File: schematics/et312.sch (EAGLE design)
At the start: 0 parts

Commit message: PCB WIP
Layed down uC and some other componants
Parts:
- added 10WAY_RIBBON: M10SILK_FEMALE_PTH, SparkFun-Connectors:M10SILK_FEMALE_PTH
- added IC1: MEGA8-P, atmel:MEGA8-P
- added S2, S4: SPST, adafruit:SPST
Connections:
- new net GND: IC1.GND, IC1.GND@1
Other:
- note added: "Menu"
- note added: "Small PCB"
- note added: "Up"
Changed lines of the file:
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@@
 <layer number="54" name="bGND_GNDA" color="1" fill="9" visible="no" active="no"/>
 <layer number="56" name="wert" color="7" fill="1" visible="no" active="no"/>
+<layer number="57" name="tCAD" color="7" fill="1" visible="no" active="no"/>
+<layer number="90" name="Modules" color="5" fill="1" visible="yes" active="yes"/>
 <layer number="91" name="Nets" color="2" fill="1" visible="yes" active="yes"/>
 <layer number="92" name="Busses" color="1" fill="1" visible="yes" active="yes"/>
@@
 <layer number="97" name="Info" color="7" fill="1" visible="yes" active="yes"/>
 <layer number="98" name="Guide" color="6" fill="1" visible="yes" active="yes"/>
+<layer number="99" name="SpiceOrder" color="7" fill="1" visible="no" active="no"/>
 <layer number="100" name="Muster" color="7" fill="1" visible="no" active="no"/>
 <layer number="101" name="Patch_Top" color="12" fill="4" visible="yes" active="yes"/>
@@
 <layer number="111" name="LPC17xx" color="7" fill="1" visible="yes" active="yes"/>
 <layer number="112" name="tSilk" color="7" fill="1" visible="yes" active="yes"/>
+<layer number="113" name="IDFDebug" color="4" fill="1" visible="yes" active="yes"/>
 <layer number="116" name="Patch_BOT" color="9" fill="4" visible="yes" active="yes"/>
 <layer number="121" name="_tsilk" color="7" fill="1" visible="yes" active="yes"/>
@@
 <layer number="132" name="bAdjust" color="7" fill="1" visible="no" active="yes"/>
 <layer number="144" name="Drill_legend" color="7" fill="1" visible="yes" active="yes"/>
+<layer number="150" name="Notes" color="7" fill="1" visible="yes" active="yes"/>
 <layer number="151" name="HeatSink" color="7" fill="1" visible="yes" active="yes"/>
 <layer number="152" name="_bDocu" color="7" fill="1" visible="yes" active="yes"/>
+<layer number="153" name="FabDoc1" color="7" fill="1" visible="yes" active="yes"/>
+<layer number="154" name="FabDoc2" color="7" fill="1" visible="yes" active="yes"/>
+<layer number="155" name="FabDoc3" color="7" fill="1" visible="yes" active="yes"/>
 <layer number="199" name="Contour" color="7" fill="1" visible="yes" active="yes"/>
 <layer number="200" name="200bmp" color="1" fill="10" visible="yes" active="yes"/>
@@
 <part name="FRAME2" library="frames" deviceset="A4L-LOC" device=""/>
 <part name="FRAME1" library="frames" deviceset="A4L-LOC" device=""/>
+<part name="IC1" library="atmel" deviceset="MEGA8-P" device=""/>
+<part name="GND1" library="SparkFun-Aesthetics" deviceset="GND" device=""/>
+<part name="FRAME3" library="frames" deviceset="A4L-LOC" device=""/>
+<part name="S2" library="adafruit" deviceset="SPST" device=""/>
+<part name="S4" library="adafruit" deviceset="SPST" device=""/>
+<part name="10WAY_RIBBON" library="SparkFun-Connectors" deviceset="M10" device="SILK_FEMALE_PTH"/>
 </parts>
 <sheets>
@@
 <instances>
 <instance part="FRAME1" gate="G$1" x="0" y="0"/>
+<instance part="IC1" gate="G$1" x="127" y="93.98"/>
+<instance part="GND1" gate="1" x="88.9" y="30.48"/>
 </instances>
 <busses>
+</busses>
+<nets>
+<net name="GND" class="0">
+<segment>
+<pinref part="GND1" gate="1" pin="GND"/>
+<wire x1="88.9" y1="33.02" x2="88.9" y2="91.44" width="0.1524" layer="91"/>
+<pinref part="IC1" gate="G$1" pin="GND@1"/>
+<wire x1="88.9" y1="91.44" x2="104.14" y2="91.44" width="0.1524" layer="91"/>
+<pinref part="IC1" gate="G$1" pin="GND"/>
+<wire x1="104.14" y1="116.84" x2="88.9" y2="116.84" width="0.1524" layer="91"/>
+<wire x1="88.9" y1="116.84" x2="88.9" y2="91.44" width="0.1524" layer="91"/>
+<junction x="88.9" y="91.44"/>
+</segment>
+</net>
+</nets>
+</sheet>
+<sheet>
+<plain>
+<text x="162.56" y="20.32" size="1.778" layer="91">Small PCB</text>
+<text x="86.36" y="134.62" size="1.778" layer="91">Menu</text>
+<text x="86.36" y="104.14" size="1.778" layer="91">Up</text>
+</plain>
+<instances>
+<instance part="FRAME3" gate="G$1" x="0" y="0"/>
+<instance part="S2" gate="G$1" x="86.36" y="142.24" rot="R270"/>
+<instance part="S4" gate="G$1" x="86.36" y="111.76" rot="R270"/>
+<instance part="10WAY_RIBBON" gate="G$1" x="12.7" y="157.48"/>
+</instances>
+<busses>

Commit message: Added small board
Added 2 buttons, and two pots to the small board, found the CD4066 in dip, and added to new sheet.
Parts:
- added 10WAY_RIBBON1: M10SILK_FEMALE_PTH, SparkFun-Connectors:M10SILK_FEMALE_PTH
- added IC2: 4066N, 40xx:4066N
- added RV1, RV2: (no value), SparkFun-Electromechanical:POT
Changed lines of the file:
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@@
 <part name="S4" library="adafruit" deviceset="SPST" device=""/>
 <part name="10WAY_RIBBON" library="SparkFun-Connectors" deviceset="M10" device="SILK_FEMALE_PTH"/>
+<part name="FRAME4" library="frames" deviceset="A4L-LOC" device=""/>
+<part name="IC2" library="40xx" deviceset="4066" device="N"/>
+<part name="10WAY_RIBBON1" library="SparkFun-Connectors" deviceset="M10" device="SILK_FEMALE_PTH"/>
+<part name="RV1" library="SparkFun-Electromechanical" deviceset="POT" device=""/>
+<part name="RV2" library="SparkFun-Electromechanical" deviceset="POT" device=""/>
 </parts>
 <sheets>
@@
 <instance part="S4" gate="G$1" x="86.36" y="111.76" rot="R270"/>
 <instance part="10WAY_RIBBON" gate="G$1" x="12.7" y="157.48"/>
+<instance part="RV1" gate="G$1" x="83.82" y="63.5"/>
+<instance part="RV2" gate="G$1" x="83.82" y="33.02"/>
 </instances>
 <busses>
+</busses>
+<nets>
+</nets>
+</sheet>
+<sheet>
+<plain>
+</plain>
+<instances>
+<instance part="FRAME4" gate="G$1" x="0" y="0"/>
+<instance part="IC2" gate="A" x="83.82" y="139.7"/>
+<instance part="IC2" gate="B" x="157.48" y="139.7"/>
+<instance part="IC2" gate="C" x="83.82" y="96.52"/>
+<instance part="IC2" gate="D" x="157.48" y="96.52"/>
+<instance part="10WAY_RIBBON1" gate="G$1" x="10.922" y="159.004"/>
+</instances>
+<busses>

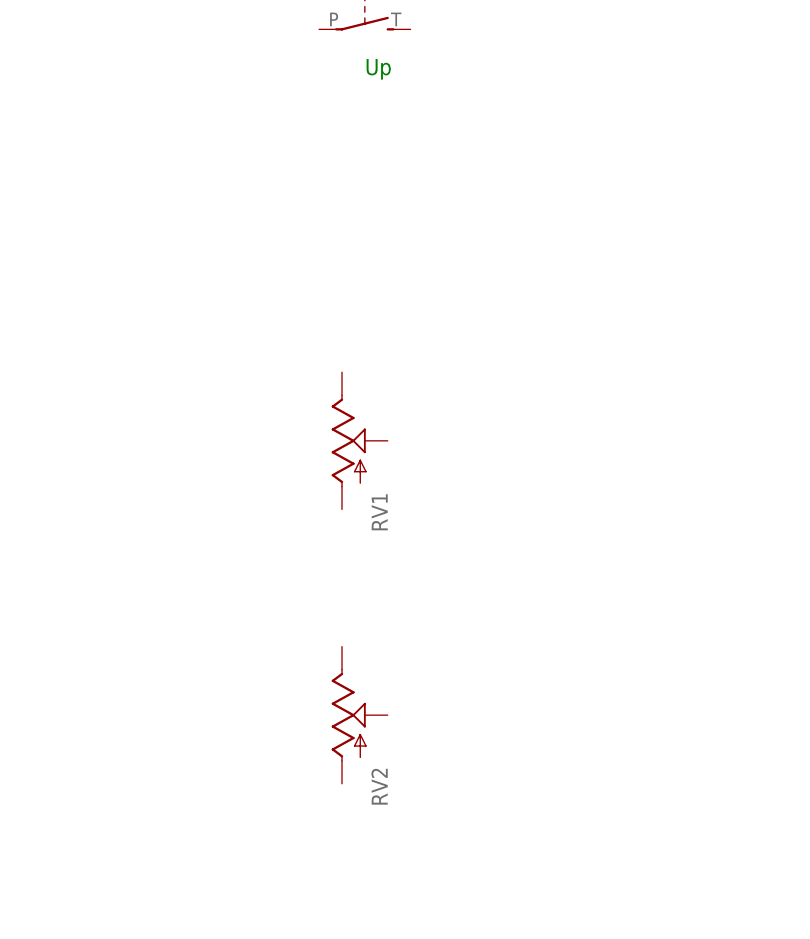
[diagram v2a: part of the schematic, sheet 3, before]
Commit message: CDB4066 added
Control pins are listed as connected to pin 22 on uC, 22 is listed as a ground… can some one please check!
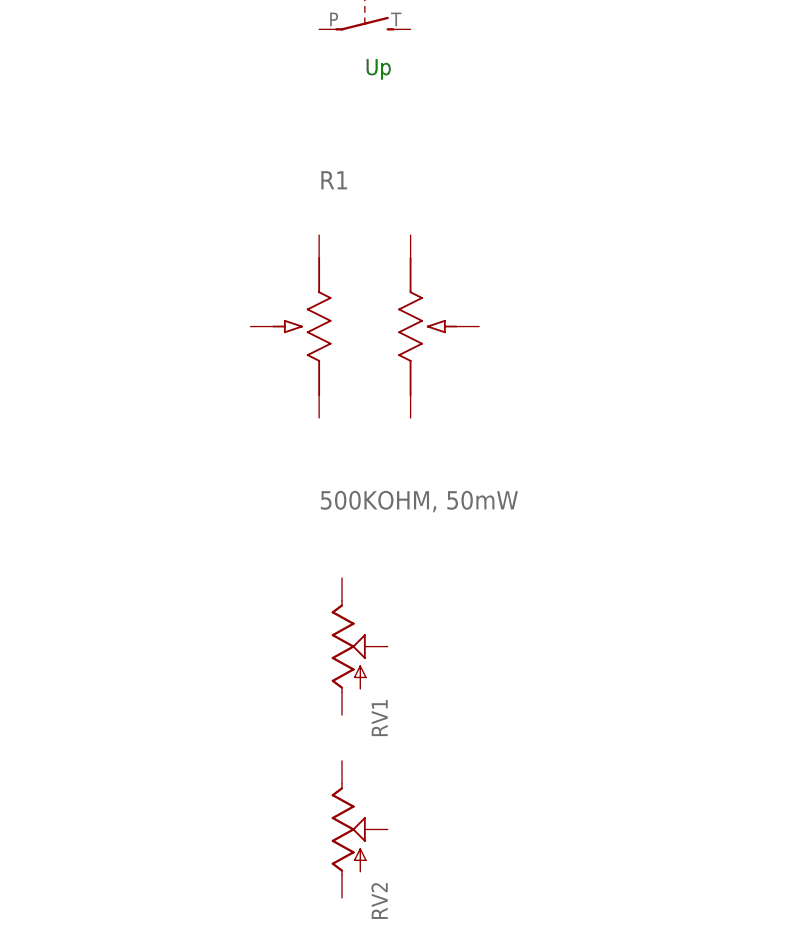
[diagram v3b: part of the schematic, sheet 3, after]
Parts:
- added R1: 500KOHM, 50mW, Panasonic-Trimmer_Potentiometers:EVJC20F02A14-JC2
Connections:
- net GND: now also IC2A.C, IC2B.C, IC2C.C, IC2D.C
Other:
- moved on the sheet: RV1, RV2
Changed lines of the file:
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@@
 <part name="RV1" library="SparkFun-Electromechanical" deviceset="POT" device=""/>
 <part name="RV2" library="SparkFun-Electromechanical" deviceset="POT" device=""/>
+<part name="R1" library="Panasonic-Trimmer_Potentiometers" deviceset="EVJ" device="-JC2" technology="C20F02A14" value="500KOHM, 50mW"/>
+<part name="GND2" library="SparkFun-Aesthetics" deviceset="GND" device=""/>
+<part name="GND3" library="SparkFun-Aesthetics" deviceset="GND" device=""/>
+<part name="GND4" library="SparkFun-Aesthetics" deviceset="GND" device=""/>
+<part name="GND5" library="SparkFun-Aesthetics" deviceset="GND" device=""/>
 </parts>
 <sheets>
@@
 <instance part="S4" gate="G$1" x="86.36" y="111.76" rot="R270"/>
 <instance part="10WAY_RIBBON" gate="G$1" x="12.7" y="157.48"/>
-<instance part="RV1" gate="G$1" x="83.82" y="63.5"/>
-<instance part="RV2" gate="G$1" x="83.82" y="33.02"/>
+<instance part="RV1" gate="G$1" x="83.82" y="40.64"/>
+<instance part="RV2" gate="G$1" x="83.82" y="20.32"/>
+<instance part="R1" gate="A" x="86.36" y="76.2"/>
 </instances>
 <busses>
@@
 <instance part="IC2" gate="D" x="157.48" y="96.52"/>
 <instance part="10WAY_RIBBON1" gate="G$1" x="10.922" y="159.004"/>
+<instance part="GND2" gate="1" x="68.58" y="86.36"/>
+<instance part="GND3" gate="1" x="68.58" y="129.54"/>
+<instance part="GND4" gate="1" x="142.24" y="129.54"/>
+<instance part="GND5" gate="1" x="142.24" y="86.36"/>
 </instances>
 <busses>
 </busses>
 <nets>
+<net name="GND" class="0">
+<segment>
+<pinref part="GND2" gate="1" pin="GND"/>
+<pinref part="IC2" gate="C" pin="C"/>
+<wire x1="68.58" y1="88.9" x2="68.58" y2="93.98" width="0.1524" layer="91"/>
+<wire x1="68.58" y1="93.98" x2="71.12" y2="93.98" width="0.1524" layer="91"/>
+</segment>
+<segment>
+<pinref part="IC2" gate="A" pin="C"/>
+<wire x1="71.12" y1="137.16" x2="68.58" y2="137.16" width="0.1524" layer="91"/>
+<pinref part="GND3" gate="1" pin="GND"/>
+<wire x1="68.58" y1="137.16" x2="68.58" y2="132.08" width="0.1524" layer="91"/>
+</segment>
+<segment>
+<pinref part="GND4" gate="1" pin="GND"/>
+<wire x1="142.24" y1="132.08" x2="142.24" y2="137.16" width="0.1524" layer="91"/>
+<pinref part="IC2" gate="B" pin="C"/>
+<wire x1="142.24" y1="137.16" x2="144.78" y2="137.16" width="0.1524" layer="91"/>
+</segment>
+<segment>
+<pinref part="IC2" gate="D" pin="C"/>
+<wire x1="144.78" y1="93.98" x2="142.24" y2="93.98" width="0.1524" layer="91"/>
+<pinref part="GND5" gate="1" pin="GND"/>
+<wire x1="142.24" y1="93.98" x2="142.24" y2="88.9" width="0.1524" layer="91"/>
+</segment>
+</net>
 </nets>
 </sheet>

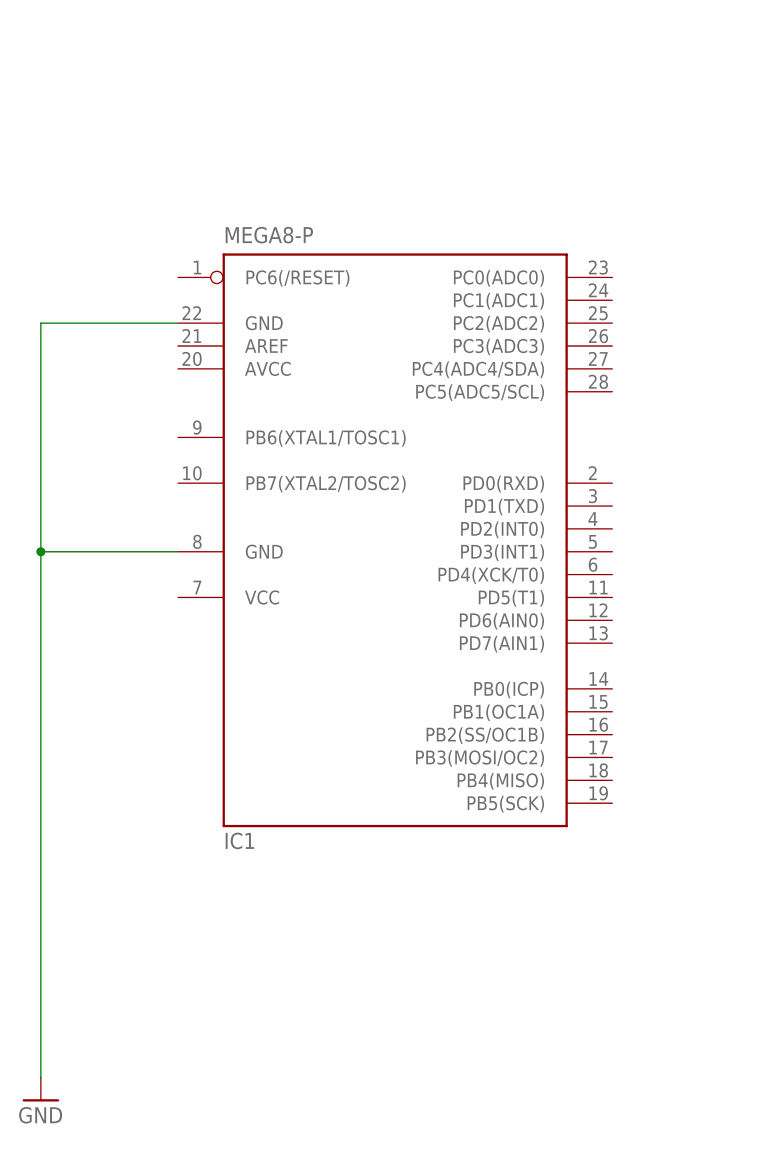
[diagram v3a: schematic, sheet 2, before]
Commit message: fixed uC
picked up a atmega16 rather than atmega8
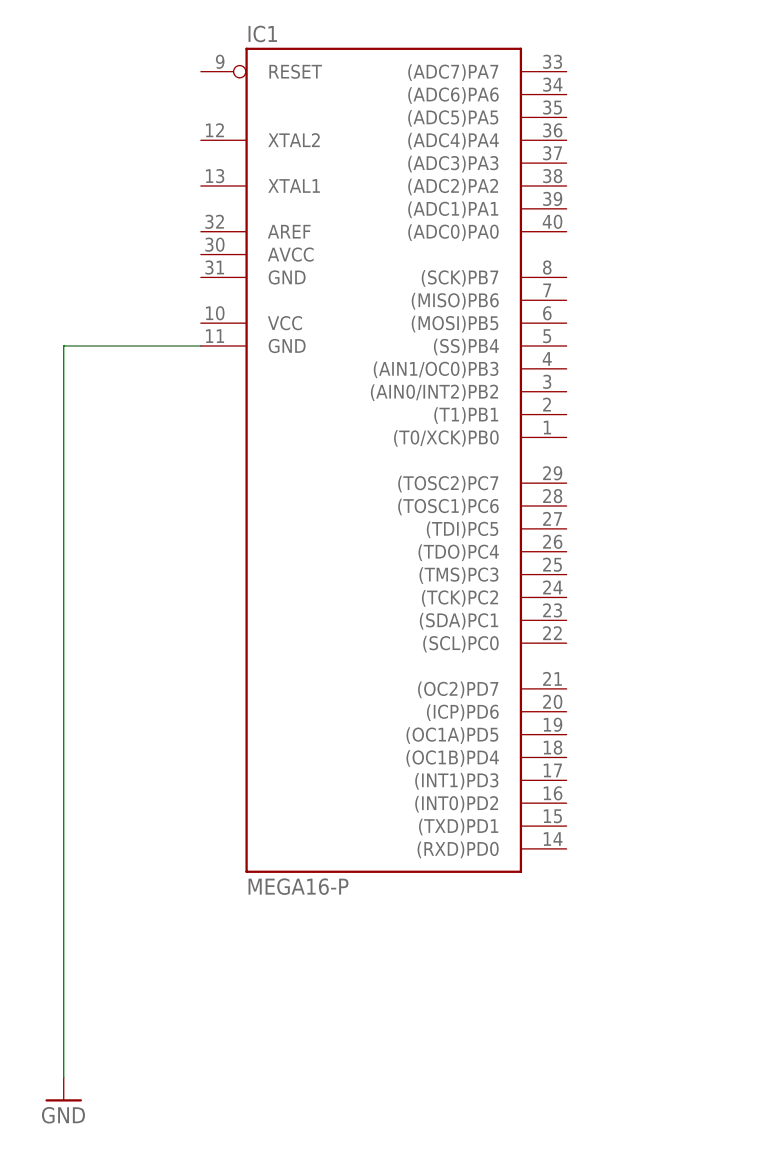
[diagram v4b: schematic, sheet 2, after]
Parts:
- IC1: value MEGA8-P -> MEGA16-P; device atmel:MEGA8-P -> atmel:MEGA16-P
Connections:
- net GND: no longer IC1.GND@1
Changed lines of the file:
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@@
 <part name="FRAME2" library="frames" deviceset="A4L-LOC" device=""/>
 <part name="FRAME1" library="frames" deviceset="A4L-LOC" device=""/>
-<part name="IC1" library="atmel" deviceset="MEGA8-P" device=""/>
 <part name="GND1" library="SparkFun-Aesthetics" deviceset="GND" device=""/>
 <part name="FRAME3" library="frames" deviceset="A4L-LOC" device=""/>
@@
 <part name="GND4" library="SparkFun-Aesthetics" deviceset="GND" device=""/>
 <part name="GND5" library="SparkFun-Aesthetics" deviceset="GND" device=""/>
+<part name="IC1" library="atmel" deviceset="MEGA16-P" device=""/>
 </parts>
 <sheets>
@@
 <instances>
 <instance part="FRAME1" gate="G$1" x="0" y="0"/>
-<instance part="IC1" gate="G$1" x="127" y="93.98"/>
-<instance part="GND1" gate="1" x="88.9" y="30.48"/>
+<instance part="GND1" gate="1" x="91.44" y="30.48"/>
+<instance part="IC1" gate="G$1" x="127" y="104.14"/>
 </instances>
 <busses>
@@
 <net name="GND" class="0">
 <segment>
+<pinref part="IC1" gate="G$1" pin="GND"/>
+<wire x1="106.68" y1="114.3" x2="91.44" y2="114.3" width="0.1524" layer="91"/>
+<wire x1="91.44" y1="114.3" x2="91.44" y2="33.02" width="0.1524" layer="91"/>
 <pinref part="GND1" gate="1" pin="GND"/>
-<wire x1="88.9" y1="33.02" x2="88.9" y2="91.44" width="0.1524" layer="91"/>
-<pinref part="IC1" gate="G$1" pin="GND@1"/>
-<wire x1="88.9" y1="91.44" x2="104.14" y2="91.44" width="0.1524" layer="91"/>
-<pinref part="IC1" gate="G$1" pin="GND"/>
-<wire x1="104.14" y1="116.84" x2="88.9" y2="116.84" width="0.1524" layer="91"/>
-<wire x1="88.9" y1="116.84" x2="88.9" y2="91.44" width="0.1524" layer="91"/>
-<junction x="88.9" y="91.44"/>
 </segment>
 </net>

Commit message: Added PDF
work done on schematic, PDF generated for people who don't have eagle.
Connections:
- new net N$1: IC2A.C
- new net N$2: IC2B.C
- new net N$3: IC2D.C
- new net N$4: IC2C.C
- net GND: no longer IC2A.C, IC2B.C, IC2C.C, IC2D.C
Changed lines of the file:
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@@
 <part name="RV2" library="SparkFun-Electromechanical" deviceset="POT" device=""/>
 <part name="R1" library="Panasonic-Trimmer_Potentiometers" deviceset="EVJ" device="-JC2" technology="C20F02A14" value="500KOHM, 50mW"/>
-<part name="GND2" library="SparkFun-Aesthetics" deviceset="GND" device=""/>
-<part name="GND3" library="SparkFun-Aesthetics" deviceset="GND" device=""/>
-<part name="GND4" library="SparkFun-Aesthetics" deviceset="GND" device=""/>
-<part name="GND5" library="SparkFun-Aesthetics" deviceset="GND" device=""/>
 <part name="IC1" library="atmel" deviceset="MEGA16-P" device=""/>
 </parts>
@@
 <sheet>
 <plain>
+</plain>
+<instances>
+<instance part="FRAME4" gate="G$1" x="0" y="0"/>
+<instance part="IC2" gate="A" x="83.82" y="139.7"/>
+<instance part="IC2" gate="B" x="157.48" y="139.7"/>
+<instance part="IC2" gate="C" x="83.82" y="96.52"/>
+<instance part="IC2" gate="D" x="157.48" y="96.52"/>
+<instance part="10WAY_RIBBON1" gate="G$1" x="10.922" y="159.004"/>
+</instances>
+<busses>
+</busses>
+<nets>
+<net name="N$1" class="0">
+<segment>
+<pinref part="IC2" gate="A" pin="C"/>
+<wire x1="71.12" y1="137.16" x2="68.58" y2="137.16" width="0.1524" layer="91"/>
+<label x="68.58" y="137.16" size="1.778" layer="95" rot="R180" xref="yes"/>
+</segment>
+</net>
+<net name="N$2" class="0">
+<segment>
+<pinref part="IC2" gate="B" pin="C"/>
+<wire x1="142.24" y1="137.16" x2="144.78" y2="137.16" width="0.1524" layer="91"/>
+<label x="142.24" y="137.16" size="1.778" layer="95" rot="R180" xref="yes"/>
+</segment>
+</net>
+<net name="N$3" class="0">
+<segment>
+<pinref part="IC2" gate="D" pin="C"/>
+<wire x1="144.78" y1="93.98" x2="142.24" y2="93.98" width="0.1524" layer="91"/>
+<label x="142.24" y="93.98" size="1.778" layer="95" rot="R180" xref="yes"/>
+</segment>
+</net>
+<net name="N$4" class="0">
+<segment>
+<pinref part="IC2" gate="C" pin="C"/>
+<wire x1="68.58" y1="93.98" x2="71.12" y2="93.98" width="0.1524" layer="91"/>
+<label x="68.58" y="93.98" size="1.778" layer="95" rot="R180" xref="yes"/>
+</segment>
+</net>
+</nets>
+</sheet>
+<sheet>
+<plain>
 <text x="162.56" y="20.32" size="1.778" layer="91">Small PCB</text>
 <text x="86.36" y="134.62" size="1.778" layer="91">Menu</text>
@@
 </nets>
 </sheet>
-<sheet>
-<plain>
-</plain>
-<instances>
-<instance part="FRAME4" gate="G$1" x="0" y="0"/>
-<instance part="IC2" gate="A" x="83.82" y="139.7"/>
-<instance part="IC2" gate="B" x="157.48" y="139.7"/>
-<instance part="IC2" gate="C" x="83.82" y="96.52"/>
-<instance part="IC2" gate="D" x="157.48" y="96.52"/>
-<instance part="10WAY_RIBBON1" gate="G$1" x="10.922" y="159.004"/>
-<instance part="GND2" gate="1" x="68.58" y="86.36"/>
-<instance part="GND3" gate="1" x="68.58" y="129.54"/>
-<instance part="GND4" gate="1" x="142.24" y="129.54"/>
-<instance part="GND5" gate="1" x="142.24" y="86.36"/>
-</instances>
-<busses>
-</busses>
-<nets>
-<net name="GND" class="0">
-<segment>
-<pinref part="GND2" gate="1" pin="GND"/>
-<pinref part="IC2" gate="C" pin="C"/>
-<wire x1="68.58" y1="88.9" x2="68.58" y2="93.98" width="0.1524" layer="91"/>
-<wire x1="68.58" y1="93.98" x2="71.12" y2="93.98" width="0.1524" layer="91"/>
-</segment>
-<segment>
-<pinref part="IC2" gate="A" pin="C"/>
-<wire x1="71.12" y1="137.16" x2="68.58" y2="137.16" width="0.1524" layer="91"/>
-<pinref part="GND3" gate="1" pin="GND"/>
-<wire x1="68.58" y1="137.16" x2="68.58" y2="132.08" width="0.1524" layer="91"/>
-</segment>
-<segment>
-<pinref part="GND4" gate="1" pin="GND"/>
-<wire x1="142.24" y1="132.08" x2="142.24" y2="137.16" width="0.1524" layer="91"/>
-<pinref part="IC2" gate="B" pin="C"/>
-<wire x1="142.24" y1="137.16" x2="144.78" y2="137.16" width="0.1524" layer="91"/>
-</segment>
-<segment>
-<pinref part="IC2" gate="D" pin="C"/>
-<wire x1="144.78" y1="93.98" x2="142.24" y2="93.98" width="0.1524" layer="91"/>
-<pinref part="GND5" gate="1" pin="GND"/>
-<wire x1="142.24" y1="93.98" x2="142.24" y2="88.9" width="0.1524" layer="91"/>
-</segment>
-</net>
-</nets>
-</sheet>
